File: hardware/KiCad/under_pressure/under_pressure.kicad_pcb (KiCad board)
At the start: 2 copper layers, 30 parts, among them J1 input, J3 output, U1 TL072, U3 TL072

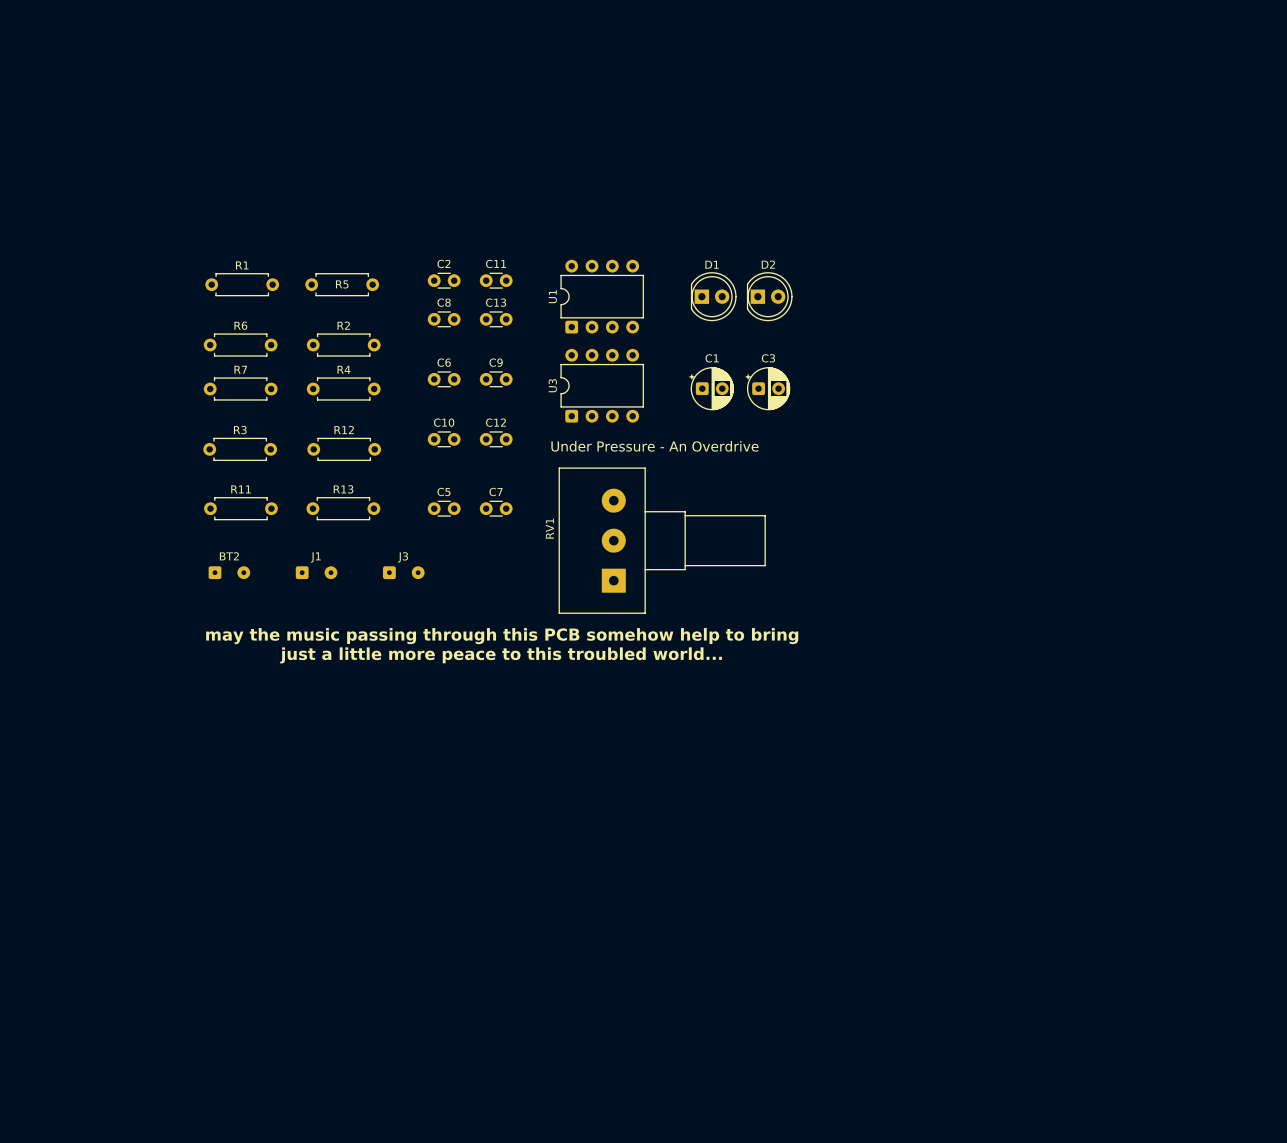
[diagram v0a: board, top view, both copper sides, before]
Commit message: cableado + esquematico arreglado
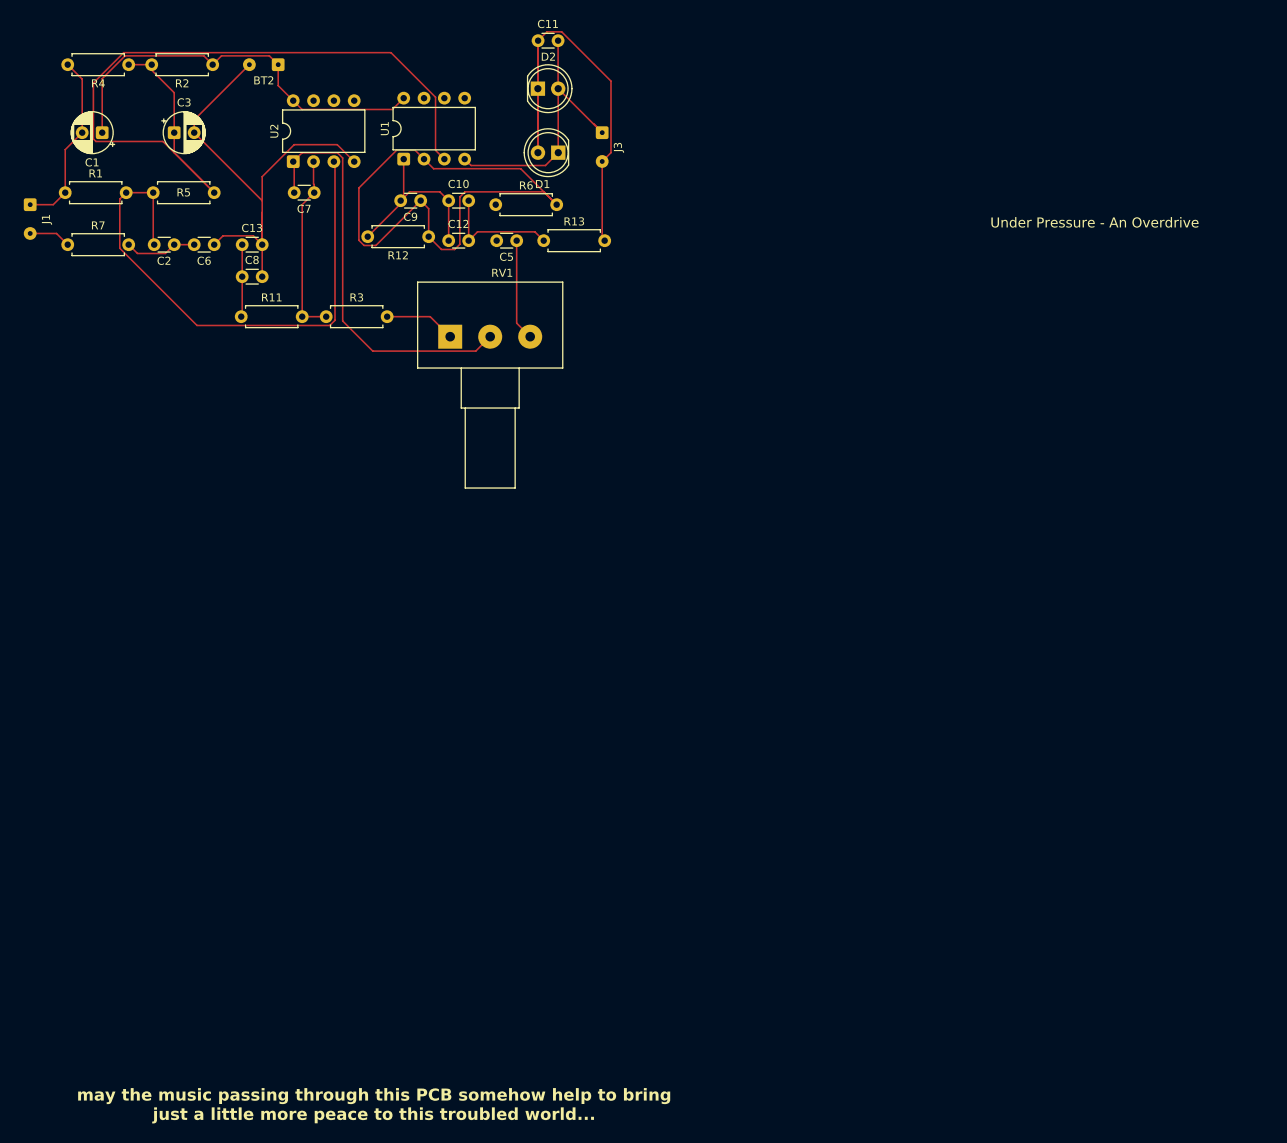
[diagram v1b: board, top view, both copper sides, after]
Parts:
- moved C1 81.6 mm to (76.0, 51.5), turned to 180 degrees
- moved C3 79.8 mm to (85.0, 51.5)
- moved BT2 64.0 mm to (98.0, 43.0), turned to 180 degrees
- moved J3 61.1 mm to (138.5, 51.5), turned to -90 degrees
- moved J1 57.2 mm to (67.0, 60.5), turned to -90 degrees
- moved U2 47.2 mm to (99.9, 55.1)
- moved R4 46.6 mm to (79.3, 43.0), turned to 180 degrees
- moved C7 45.0 mm to (102.5, 59.0), turned to 180 degrees
- moved R13 44.2 mm to (131.2, 65.0)
- moved R6 39.8 mm to (125.2, 60.5)
- moved D2 37.8 mm to (130.5, 46.0)
- moved R2 37.2 mm to (89.8, 43.0), turned to 180 degrees
- moved RV1 36.7 mm to (119.5, 77.0), turned to 90 degrees
- moved C5 35.1 mm to (127.8, 65.0), turned to 180 degrees
- moved C2 32.8 mm to (85.0, 65.5), turned to 180 degrees
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- renumbered U3 to U2
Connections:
- U1 pad 4: (no net) -> GND
- U1 pad 8: (no net) -> Net-(BT2-+)
- U2 pad 4: (no net) -> GND
- U2 pad 8: (no net) -> Net-(BT2-+)
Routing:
- net GND: track 0.00 -> 119.6 mm
- net Net-(U1A-+): track 0.46 -> 101.8 mm
- net Net-(U1A--): track 0.00 -> 75.0 mm
- net Net-(U2A-+): track 0.00 -> 68.3 mm
- net Net-(D1-A): track 0.00 -> 60.7 mm
- net Net-(C7-Pad2): track 0.00 -> 52.0 mm
- net Net-(BT2-+): track 0.00 -> 51.4 mm
- net Net-(C10-Pad1): track 0.00 -> 23.9 mm
- net Net-(U2A--): track 0.00 -> 23.0 mm
- net Net-(C10-Pad2): track 0.00 -> 15.3 mm
- net Net-(C5-Pad1): track 0.00 -> 13.2 mm
- net Net-(C2-Pad1): track 0.00 -> 9.10 mm
- net Net-(C13-Pad1): track 0.00 -> 9.05 mm
- net Net-(R3-Pad2): track 0.00 -> 8.92 mm
- net Net-(J1-PadT): track 0.00 -> 5.27 mm

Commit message: gerbers
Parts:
- R8: renamed from R3; value 680kΩ -> 2.2kΩ
- moved J1 71.2 mm to (119.5, 108.5)
- moved R7 69.7 mm to (120.7, 115.0)
- moved R8 69.4 mm to (160.0, 115.5), turned to -90 degrees
- moved U1 69.2 mm to (165.5, 100.6)
- moved R11 68.6 mm to (148.4, 115.5)
- moved C7 68.0 mm to (152.0, 105.5)
- moved D1 67.6 mm to (182.6, 100.0)
- moved C1 67.6 mm to (125.5, 97.5)
- moved R1 67.6 mm to (120.9, 105.0)
- moved C10 67.6 mm to (168.8, 106.0)
- moved C11 67.6 mm to (180.0, 86.0)
- moved C12 67.6 mm to (168.8, 111.0)
- moved C13 67.6 mm to (143.0, 111.5)
- moved C2 67.6 mm to (134.5, 111.5)
- moved C3 67.6 mm to (134.5, 97.5)
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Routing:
- net GND: track 119.6 -> 209.3 mm
- net Net-(U1A--): track 75.0 -> 28.2 mm
- net Net-(U2A-+): track 68.3 -> 36.0 mm
- net Net-(D1-A): track 60.7 -> 33.3 mm
- net Net-(C7-Pad2): track 52.0 -> 40.2 mm
- net Net-(C10-Pad1): track 23.9 -> 33.9 mm
- net Net-(BT2-+): track 51.4 -> 58.0 mm
- net Net-(U1A-+): track 101.8 -> 95.8 mm
- net Net-(C5-Pad2): track 0.00 -> 4.55 mm
- net Net-(U2A--): track 23.0 -> 20.9 mm
- net Net-(J1-PadT): track 5.27 -> 3.24 mm
- net Net-(C10-Pad2): track 15.3 -> 17.3 mm
- net Net-(C2-Pad1): track 9.10 -> 10.8 mm
- net Net-(C13-Pad1): track 9.05 -> 10.3 mm
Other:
- board outline added: 74 x 44.5 mm
- board text added: "U2"
- board text added: "Under Pressure"
- board text removed: "Under Pressure - An Overdrive"
